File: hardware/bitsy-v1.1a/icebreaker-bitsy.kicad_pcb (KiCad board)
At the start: 4 copper layers, 35.6 x 17.8 mm, 99 parts, among them J1 USB_C, P0 0, P1 1, P10 10, P11 11, P12 12, P13 13, P14 14, P15 15, P16 16, P17 17, P18 18, P19 19, P2 2, P20 20, P21 21, P22 22, P23 23, P24 GND, P25 GND, P26 GND, P27 3V3, P28 3V3, P29 VIN, P3 3, P30 CDONE, P31 CRESET, P32 UP, P33 UP, P34 UP, P35 UP, P36 CS, P37 SCK, P38 MISO, P39 MOSI, P4 4, P40 IO3, P41 IO2, P5 5, P6 6, P7 7, P8 8, P9 9, SW1 TACT, U1 USBLC6-2, U2 TLV75533PDRV, U3 TLV75512PDRV, U4 LY68L6400, U5 W25Q128JVxxM, U6 ICE40UP5K-SG48, X1 12MHz

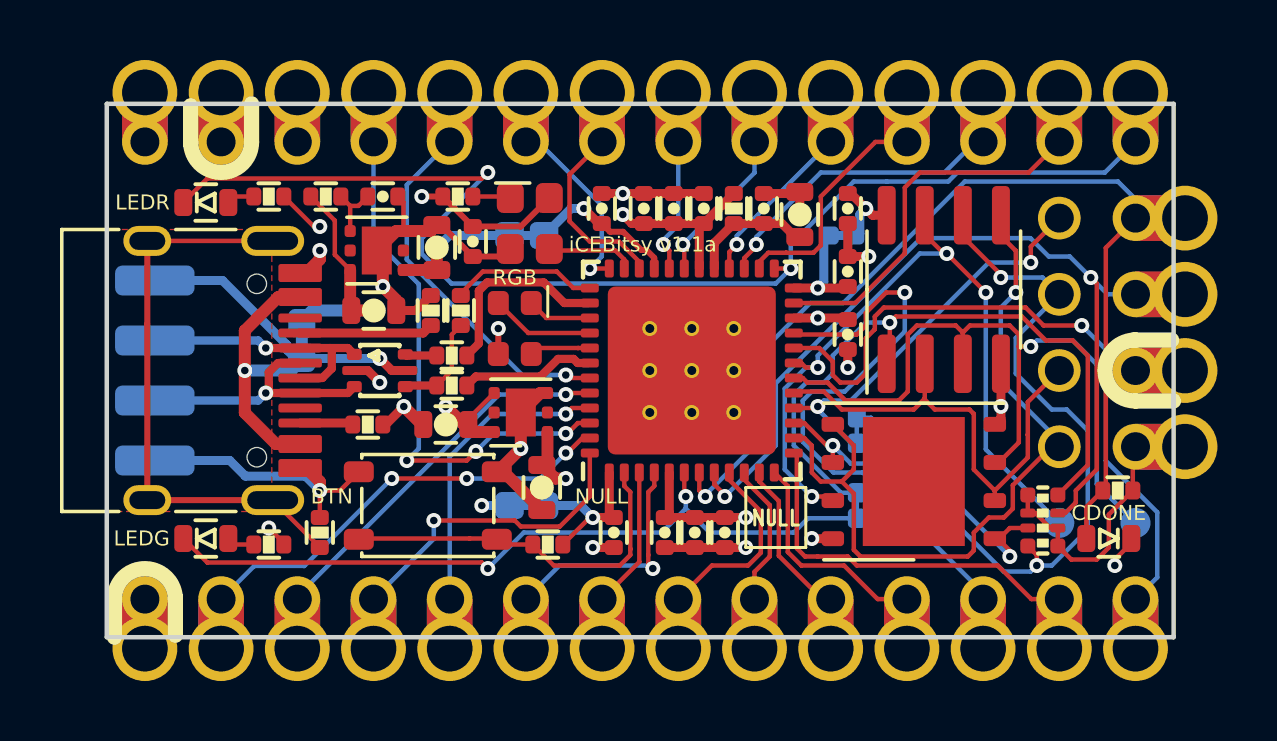
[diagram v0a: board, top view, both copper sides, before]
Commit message: Updated all design files to KiCad V8.0.6.
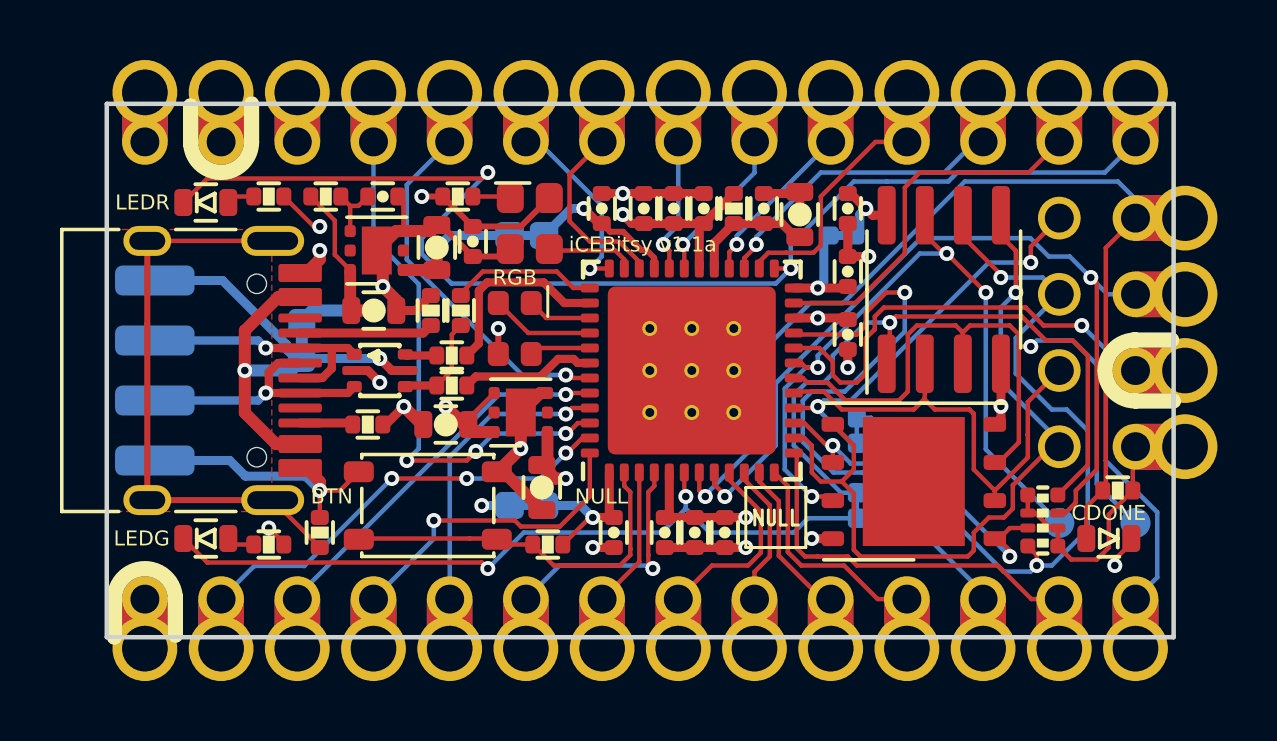
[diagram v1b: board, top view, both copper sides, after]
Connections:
- net /FLASH_~CS renamed /FLASH_~{CS}
- net /IOB_13b-~LEDG renamed /IOB_13b-~{LEDG}
- net /IOT_36b-~LEDR renamed /IOT_36b-~{LEDR}
- net /RAM_~CS renamed /RAM_~{CS}
- net /SPI_~CS renamed /SPI_~{CS}
- net /SPI_~HLD~-IO3 renamed /SPI_~{HLD}-IO3
- net /SPI_~WP~-IO2 renamed /SPI_~{WP}-IO2
- net /~BTN renamed /~{BTN}
- net /~CRESET renamed /~{CRESET}
- net /~RGB0 renamed /~{RGB0}
- net /~RGB1 renamed /~{RGB1}
- net /~RGB2 renamed /~{RGB2}
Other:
- net class Default removed
- net class S50 removed
- net class USB-D90 removed
- board text added: "13 25 IOT_36b- ~{LEDR}"
- board text added: "~{CRESET}"
- board text added: "~{CS}"
- board text removed: "13 25 IOT_36b- ~LEDR"
- board text removed: "~CRESET"
- board text removed: "~CS"
